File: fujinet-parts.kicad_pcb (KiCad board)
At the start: 2 copper layers, 1 part

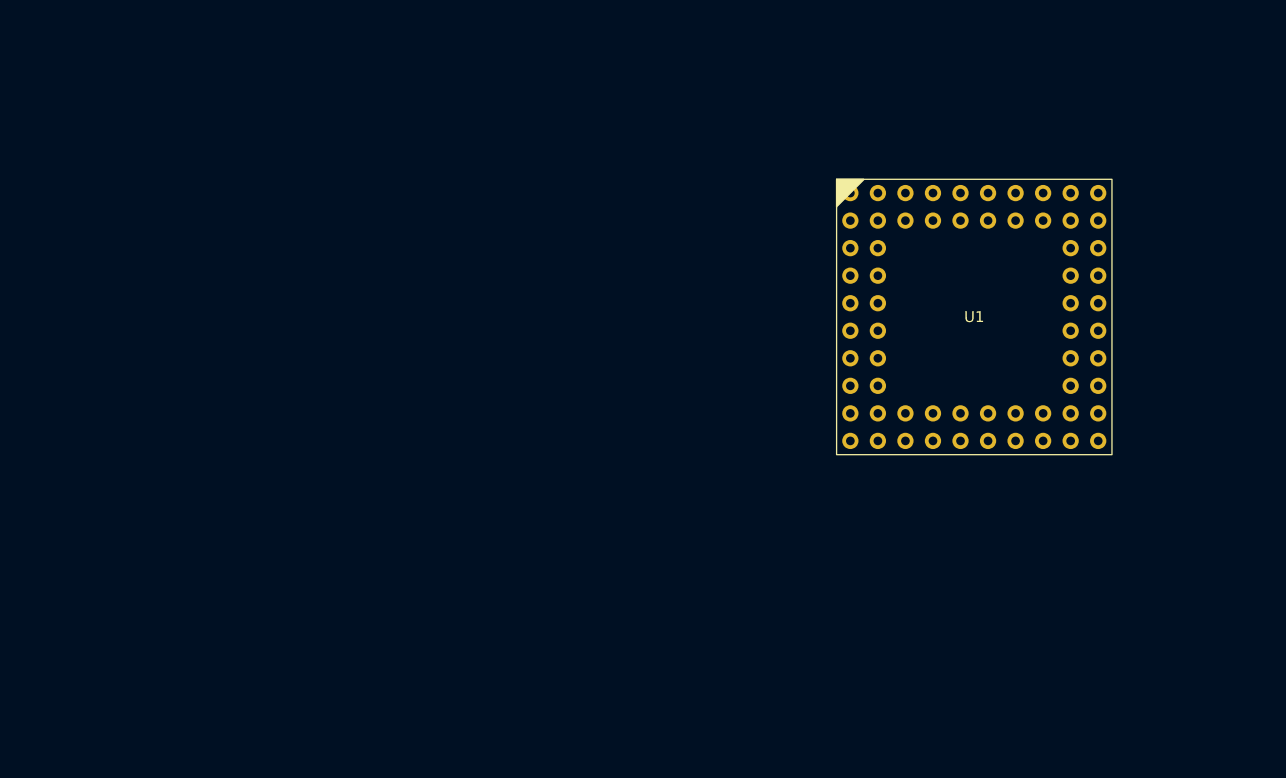
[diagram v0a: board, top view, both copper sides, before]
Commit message: ESP32-S3-CAM
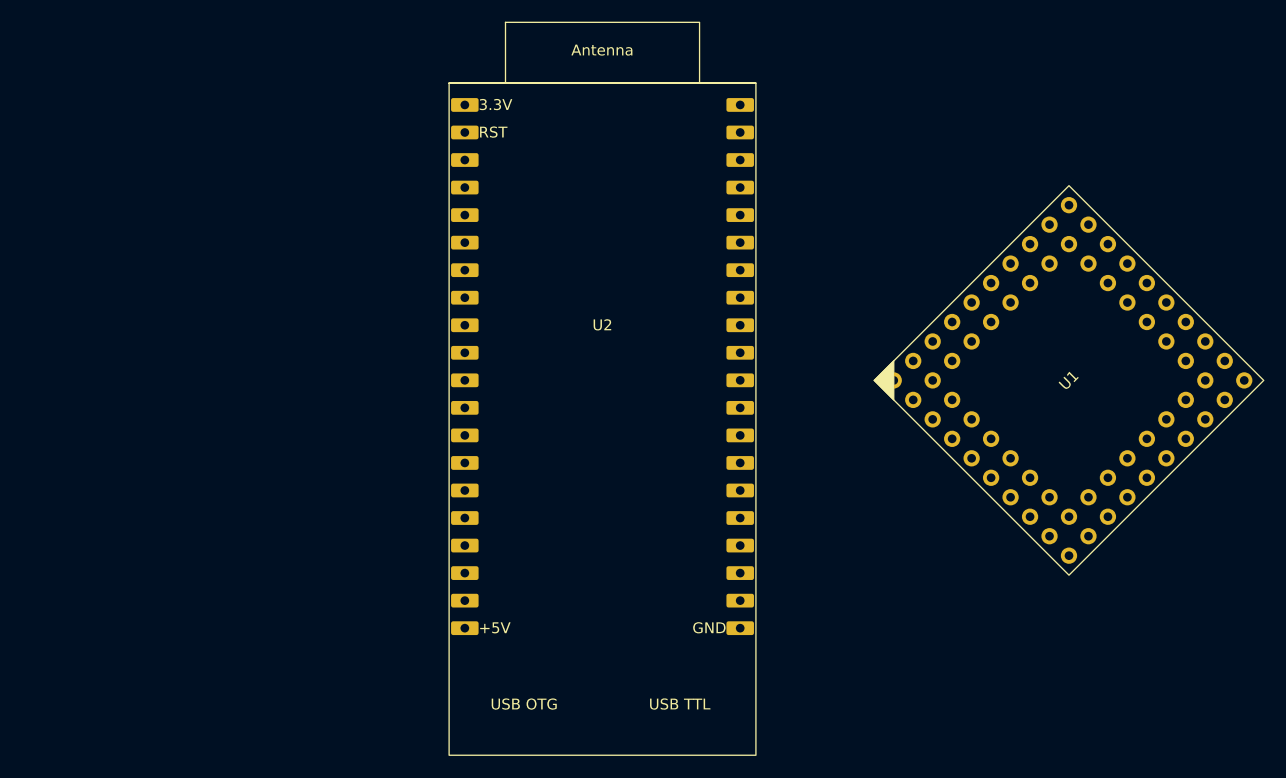
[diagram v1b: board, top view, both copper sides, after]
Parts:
- added U2: ~, FujiNet:ESP32-S3-CAM, F.Cu at (177.3, 92.5)
- turned U1 to 45 degrees

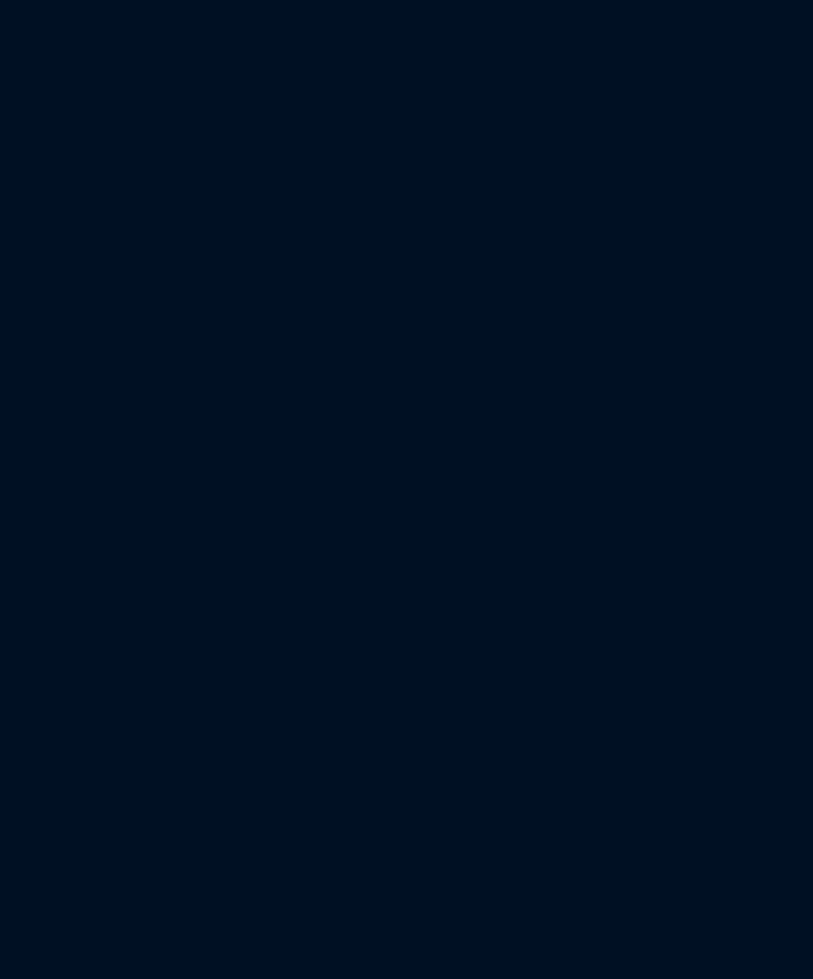
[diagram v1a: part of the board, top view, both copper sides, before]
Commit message: Link 98357A symbol and footprint
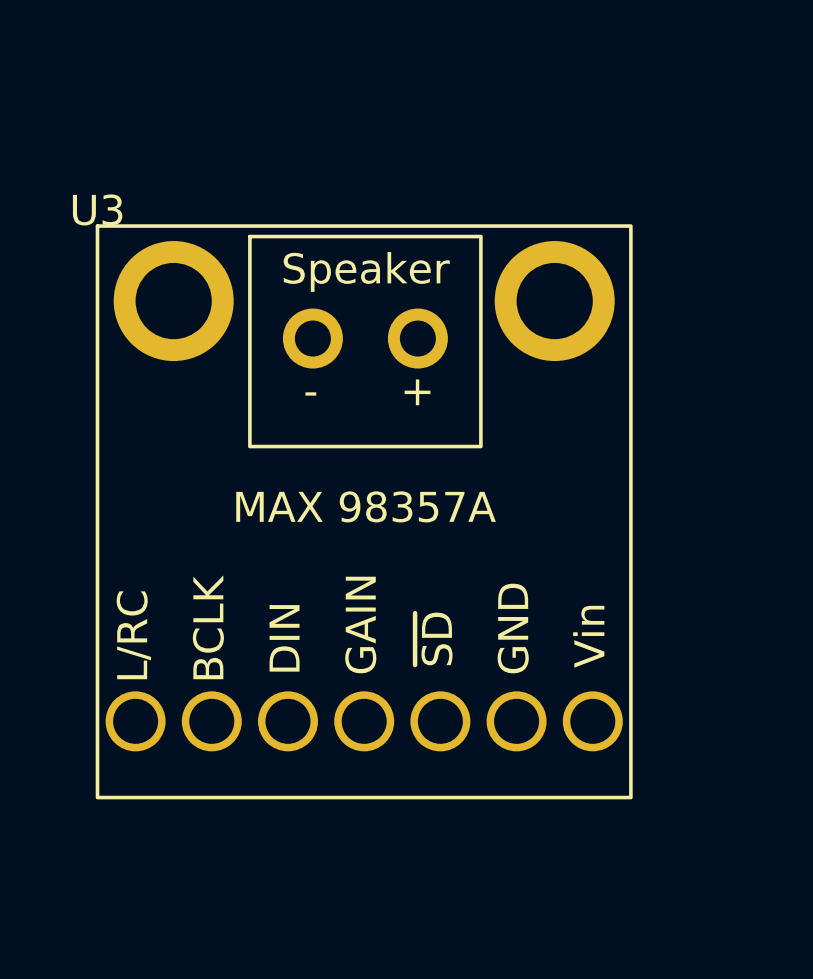
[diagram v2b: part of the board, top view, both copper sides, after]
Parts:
- added U3: ~, FujiNet:MAX98357A_i2c_Breakout, F.Cu at (155.4, 123.4)
